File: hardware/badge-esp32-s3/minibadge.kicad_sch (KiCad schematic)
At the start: 10 parts, among them J10 Conn_01x02_Socket, J3 Conn_01x02_Socket, J4 Conn_01x02_Socket, J5 Conn_01x02_Socket, J6 Conn_01x04_Socket, J7 Conn_01x02_Socket, J8 Conn_01x04_Socket, J9 Conn_01x02_Socket

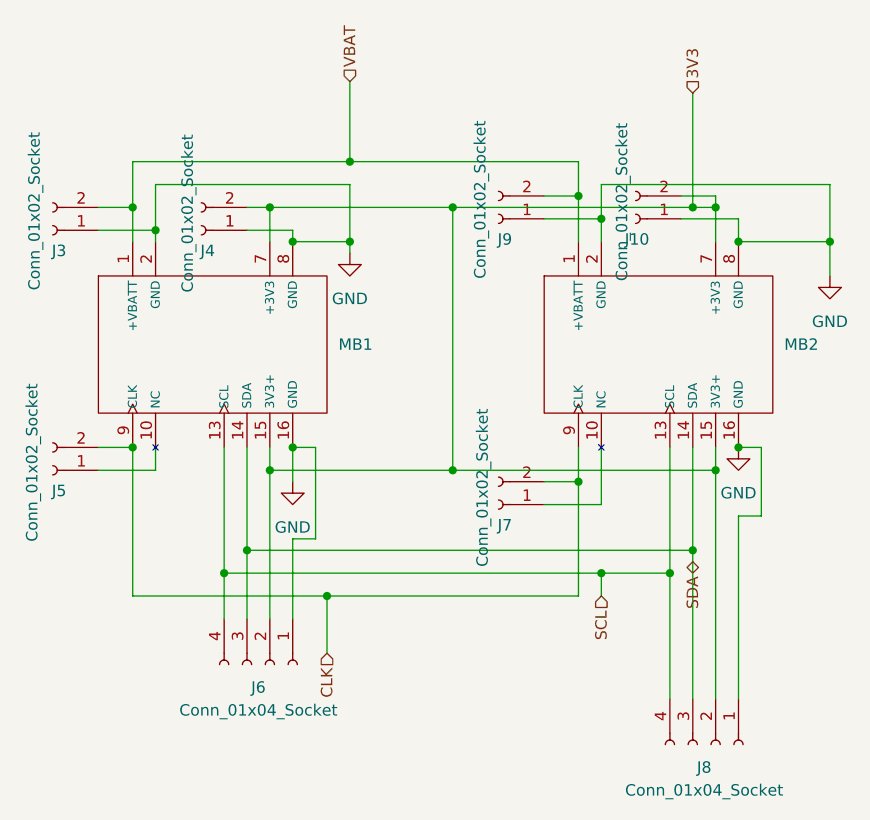
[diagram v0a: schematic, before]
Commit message: Added capacitors and inductors for the buck boost converter.
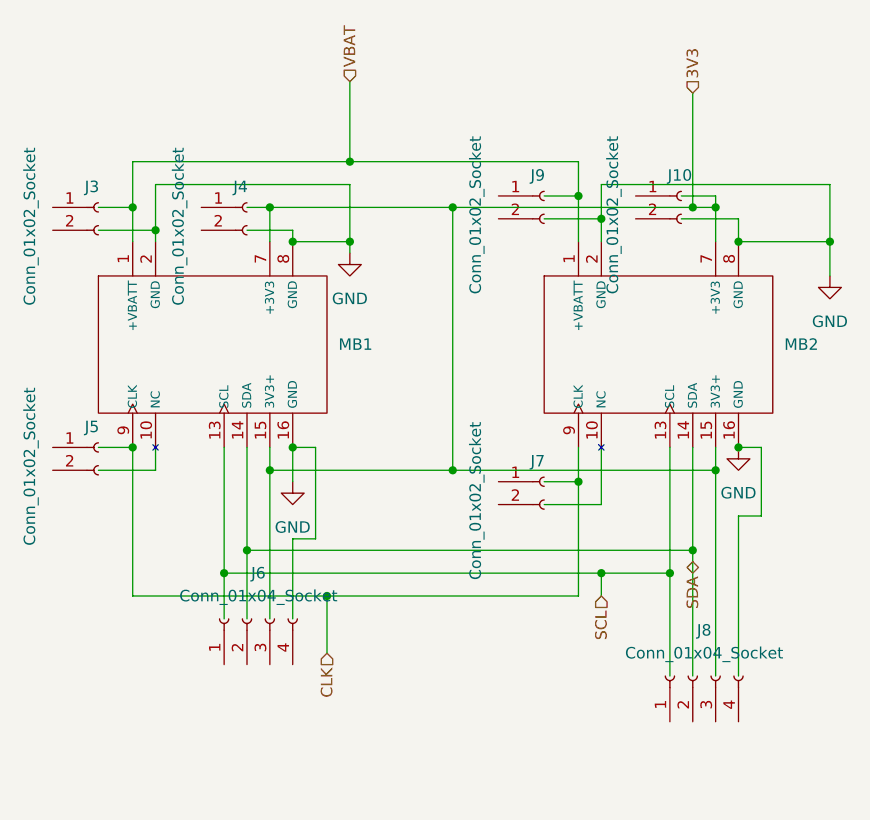
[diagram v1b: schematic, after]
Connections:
- net 3V3: no longer J10.2 (Pin_2), J4.2 (Pin_2), J6.2 (Pin_2), J8.2 (Pin_2)
- net CLK: no longer J5.2 (Pin_2), J7.2 (Pin_2)
- net GND: no longer J10.1 (Pin_1), J3.1 (Pin_1), J4.1 (Pin_1), J6.1 (Pin_1), J8.1 (Pin_1), J9.1 (Pin_1)
- net SCL: no longer J6.4 (Pin_4), J8.4 (Pin_4)
- net SDA: no longer J6.3 (Pin_3), J8.3 (Pin_3)
- net VBAT: no longer J3.2 (Pin_2), J9.2 (Pin_2)
- net at J5.1 (Pin_1): no longer MB1.10 (NC)
- net at J7.1 (Pin_1): no longer MB2.10 (NC)
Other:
- moved on the sheet: J10, J3, J4, J5, J6, J7, J8, J9
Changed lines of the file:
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@@
-	(wire
-		(pts
-			(xy 154.94 100.33) (xy 154.94 114.3)
-		)
-		(stroke
-			(width 0)
-			(type default)
-		)
-	)
 	(wire
 		(pts
@@
 	(wire
 		(pts
-			(xy 157.48 97.79) (xy 157.48 114.3)
-		)
-		(stroke
-			(width 0)
-			(type default)
-		)
-	)
-	(wire
-		(pts
 			(xy 160.02 59.69) (xy 160.02 63.5)
 		)
@@
 	(wire
 		(pts
-			(xy 162.56 93.98) (xy 162.56 114.3)
-		)
-		(stroke
-			(width 0)
-			(type default)
-		)
-	)
-	(wire
-		(pts
 			(xy 113.03 105.41) (xy 113.03 96.52)
 		)
@@
 	(wire
 		(pts
+			(xy 154.94 100.33) (xy 154.94 111.76)
+		)
+		(stroke
+			(width 0)
+			(type default)
+		)
+	)
+	(wire
+		(pts
 			(xy 147.32 57.15) (xy 172.72 57.15)
 		)
@@
 	(wire
 		(pts
+			(xy 157.48 97.79) (xy 157.48 111.76)
+		)
+		(stroke
+			(width 0)
+			(type default)
+		)
+	)
+	(wire
+		(pts
 			(xy 165.1 93.98) (xy 165.1 86.36)
 		)
@@
 	(wire
 		(pts
-			(xy 160.02 88.9) (xy 160.02 114.3)
+			(xy 162.56 93.98) (xy 162.56 111.76)
 		)
 		(stroke
@@
 		(pts
 			(xy 105.41 100.33) (xy 147.32 100.33)
+		)
+		(stroke
+			(width 0)
+			(type default)
+		)
+	)
+	(wire
+		(pts
+			(xy 160.02 88.9) (xy 160.02 111.76)
 		)
 		(stroke
@@
 	(symbol
 		(lib_id "Connector:Conn_01x02_Socket")
-		(at 86.36 88.9 180)
+		(at 91.44 86.36 0)
 		(unit 1)
 		(exclude_from_sim no)
@@
 		(dnp no)
 		(property "Reference" "J5"
-			(at 87.884 91.186 0)
+			(at 89.916 84.074 0)
 			(effects
 				(font
@@
 		)
 		(property "Value" "Conn_01x02_Socket"
-			(at 84.074 79.248 90)
+			(at 83.82 97.282 90)
 			(effects
 				(font
@@
 		)
 		(property "Footprint" "Connector_PinHeader_2.54mm:PinHeader_1x02_P2.54mm_Vertical"
-			(at 86.36 88.9 0)
+			(at 91.44 86.36 0)
 			(effects
 				(font
@@
 		)
 		(property "Datasheet" "~"
-			(at 86.36 88.9 0)
+			(at 91.44 86.36 0)
 			(effects
 				(font
@@
 		)
 		(property "Description" "Generic connector, single row, 01x02, script generated"
-			(at 86.36 88.9 0)
+			(at 91.44 86.36 0)
 			(effects
 				(font
@@
 	(symbol
 		(lib_id "Connector:Conn_01x02_Socket")
-		(at 135.89 92.71 180)
+		(at 140.97 90.17 0)
 		(unit 1)
 		(exclude_from_sim no)
@@
 		(dnp no)
 		(property "Reference" "J7"
-			(at 137.414 94.996 0)
+			(at 139.446 87.884 0)
 			(effects
 				(font
@@
 		)
 		(property "Value" "Conn_01x02_Socket"
-			(at 134.112 82.042 90)
+			(at 133.35 101.092 90)
 			(effects
 				(font
@@
 		)
 		(property "Footprint" "Connector_PinHeader_2.54mm:PinHeader_1x02_P2.54mm_Vertical"
-			(at 135.89 92.71 0)
+			(at 140.97 90.17 0)
 			(effects
 				(font
@@
 		)
 		(property "Datasheet" "~"
-			(at 135.89 92.71 0)
+			(at 140.97 90.17 0)
 			(effects
 				(font
@@
 		)
 		(property "Description" "Generic connector, single row, 01x02, script generated"
-			(at 135.89 92.71 0)
+			(at 140.97 90.17 0)
 			(effects
 				(font
@@
 	(symbol
 		(lib_id "Connector:Conn_01x02_Socket")
-		(at 86.36 62.23 180)
+		(at 91.44 59.69 0)
 		(unit 1)
 		(exclude_from_sim no)
@@
 		(dnp no)
 		(property "Reference" "J3"
-			(at 87.884 64.516 0)
+			(at 89.916 57.404 0)
 			(effects
 				(font
@@
 		)
 		(property "Value" "Conn_01x02_Socket"
-			(at 84.328 51.308 90)
+			(at 83.82 70.612 90)
 			(effects
 				(font
@@
 		)
 		(property "Footprint" "Connector_PinHeader_2.54mm:PinHeader_1x02_P2.54mm_Vertical"
-			(at 86.36 62.23 0)
+			(at 91.44 59.69 0)
 			(effects
 				(font
@@
 		)
 		(property "Datasheet" "~"
-			(at 86.36 62.23 0)
+			(at 91.44 59.69 0)
 			(effects
 				(font
@@
 		)
 		(property "Description" "Generic connector, single row, 01x02, script generated"
-			(at 86.36 62.23 0)
+			(at 91.44 59.69 0)
 			(effects
 				(font
@@
 		)
 		(instances
-			(project "badge-esp32-s3"
+			(project ""
 				(path "/e2af9a6c-dbe9-4de2-9ba6-ea213a7300ec/18b0dd1f-1411-4aae-8334-5d13e6c2c6f9"
 					(reference "J3")
@@
 	(symbol
 		(lib_id "Connector:Conn_01x02_Socket")
-		(at 151.13 60.96 180)
+		(at 156.21 58.42 0)
 		(unit 1)
 		(exclude_from_sim no)
@@
 		(dnp no)
 		(property "Reference" "J10"
-			(at 152.654 63.246 0)
+			(at 154.686 56.134 0)
 			(effects
 				(font
@@
 		)
 		(property "Value" "Conn_01x02_Socket"
-			(at 149.606 50.292 90)
+			(at 148.59 69.342 90)
 			(effects
 				(font
@@
 		)
 		(property "Footprint" "Connector_PinHeader_2.54mm:PinHeader_1x02_P2.54mm_Vertical"
-			(at 151.13 60.96 0)
+			(at 156.21 58.42 0)
 			(effects
 				(font
@@
 		)
 		(property "Datasheet" "~"
-			(at 151.13 60.96 0)
+			(at 156.21 58.42 0)
 			(effects
 				(font
@@
 		)
 		(property "Description" "Generic connector, single row, 01x02, script generated"
-			(at 151.13 60.96 0)
+			(at 156.21 58.42 0)
 			(effects
 				(font
@@
 	(symbol
 		(lib_id "Connector:Conn_01x04_Socket")
-		(at 110.49 110.49 270)
+		(at 107.95 105.41 90)
 		(unit 1)
 		(exclude_from_sim no)
@@
 		(fields_autoplaced yes)
 		(property "Reference" "J6"
-			(at 109.22 113.03 90)
+			(at 109.22 100.33 90)
 			(effects
 				(font
@@
 		)
 		(property "Value" "Conn_01x04_Socket"
-			(at 109.22 115.57 90)
+			(at 109.22 102.87 90)
 			(effects
 				(font
@@
 		)
 		(property "Footprint" "Connector_PinHeader_2.54mm:PinHeader_1x04_P2.54mm_Vertical"
-			(at 110.49 110.49 0)
+			(at 107.95 105.41 0)
 			(effects
 				(font
@@
 		)
 		(property "Datasheet" "~"
-			(at 110.49 110.49 0)
+			(at 107.95 105.41 0)
 			(effects
 				(font
@@
 		)
 		(property "Description" "Generic connector, single row, 01x04, script generated"
-			(at 110.49 110.49 0)
+			(at 107.95 105.41 0)
 			(effects
 				(font
@@
 		)
 		(instances
-			(project "badge-esp32-s3"
+			(project ""
 				(path "/e2af9a6c-dbe9-4de2-9ba6-ea213a7300ec/18b0dd1f-1411-4aae-8334-5d13e6c2c6f9"
 					(reference "J6")
@@
 	(symbol
 		(lib_id "Connector:Conn_01x02_Socket")
-		(at 102.87 62.23 180)
+		(at 107.95 59.69 0)
 		(unit 1)
 		(exclude_from_sim no)
@@
 		(dnp no)
 		(property "Reference" "J4"
-			(at 104.394 64.516 0)
+			(at 106.426 57.404 0)
 			(effects
 				(font
@@
 		)
 		(property "Value" "Conn_01x02_Socket"
-			(at 101.346 51.562 90)
+			(at 100.33 70.612 90)
 			(effects
 				(font
@@
 		)
 		(property "Footprint" "Connector_PinHeader_2.54mm:PinHeader_1x02_P2.54mm_Vertical"
-			(at 102.87 62.23 0)
+			(at 107.95 59.69 0)
 			(effects
 				(font
@@
 		)
 		(property "Datasheet" "~"
-			(at 102.87 62.23 0)
+			(at 107.95 59.69 0)
 			(effects
 				(font
@@
 		)
 		(property "Description" "Generic connector, single row, 01x02, script generated"
-			(at 102.87 62.23 0)
+			(at 107.95 59.69 0)
 			(effects
 				(font
@@
 	(symbol
 		(lib_id "Connector:Conn_01x02_Socket")
-		(at 135.89 60.96 180)
+		(at 140.97 58.42 0)
 		(unit 1)
 		(exclude_from_sim no)
@@
 		(dnp no)
 		(property "Reference" "J9"
-			(at 137.414 63.246 0)
+			(at 139.446 56.134 0)
 			(effects
 				(font
@@
 		)
 		(property "Value" "Conn_01x02_Socket"
-			(at 133.858 50.038 90)
+			(at 133.35 69.342 90)
 			(effects
 				(font
@@
 		)
 		(property "Footprint" "Connector_PinHeader_2.54mm:PinHeader_1x02_P2.54mm_Vertical"
-			(at 135.89 60.96 0)
+			(at 140.97 58.42 0)
 			(effects
 				(font
@@
 		)
 		(property "Datasheet" "~"
-			(at 135.89 60.96 0)
+			(at 140.97 58.42 0)
 			(effects
 				(font
@@
 		)
 		(property "Description" "Generic connector, single row, 01x02, script generated"
-			(at 135.89 60.96 0)
+			(at 140.97 58.42 0)
 			(effects
 				(font
@@
 	(symbol
 		(lib_id "Connector:Conn_01x04_Socket")
-		(at 160.02 119.38 270)
+		(at 157.48 111.76 90)
 		(unit 1)
 		(exclude_from_sim no)
@@
 		(fields_autoplaced yes)
 		(property "Reference" "J8"
-			(at 158.75 121.92 90)
+			(at 158.75 106.68 90)
 			(effects
 				(font
@@
 		)
 		(property "Value" "Conn_01x04_Socket"
-			(at 158.75 124.46 90)
+			(at 158.75 109.22 90)
 			(effects
 				(font
@@
 		)
 		(property "Footprint" "Connector_PinHeader_2.54mm:PinHeader_1x04_P2.54mm_Vertical"
-			(at 160.02 119.38 0)
+			(at 157.48 111.76 0)
 			(effects
 				(font
@@
 		)
 		(property "Datasheet" "~"
-			(at 160.02 119.38 0)
+			(at 157.48 111.76 0)
 			(effects
 				(font
@@
 		)
 		(property "Description" "Generic connector, single row, 01x04, script generated"
-			(at 160.02 119.38 0)
-			(effects
-				(font
+			(at 157.48 111.76 0)
+			(effects
+				(font
